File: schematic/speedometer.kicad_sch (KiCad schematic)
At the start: 11 parts

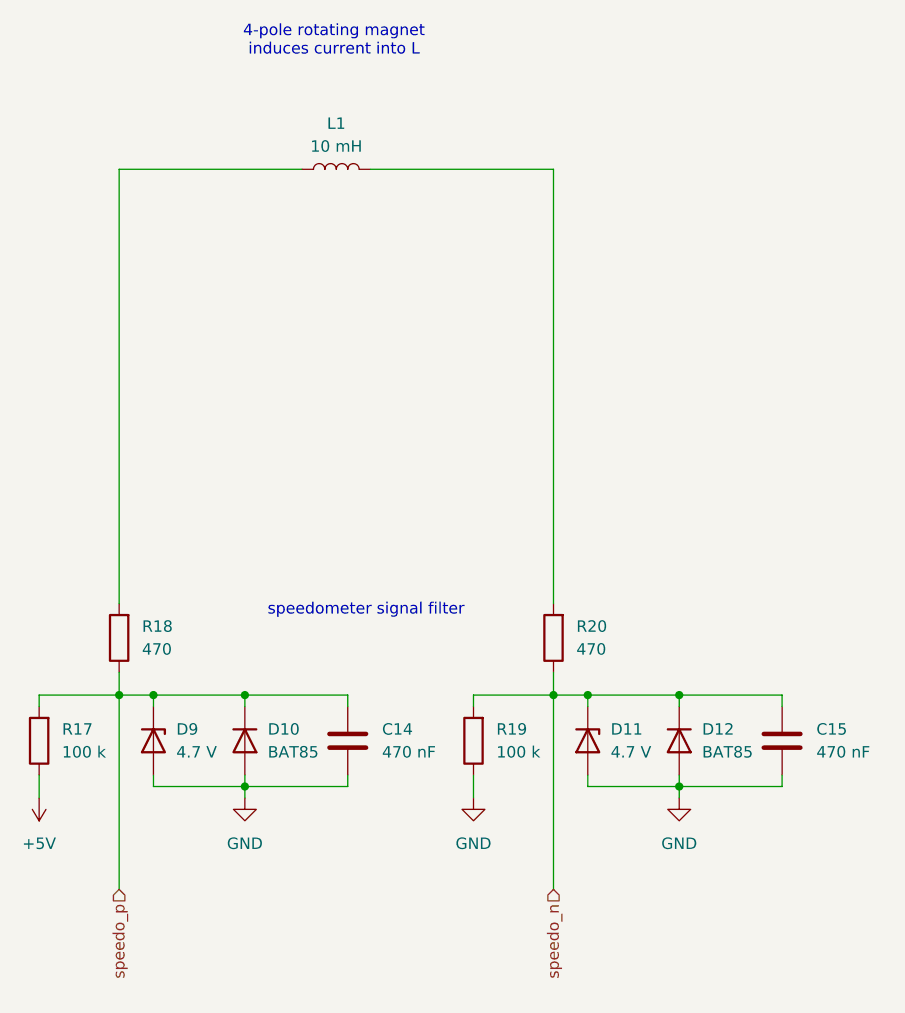
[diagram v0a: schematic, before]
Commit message: schematic: Add 2nd shutoff biasing
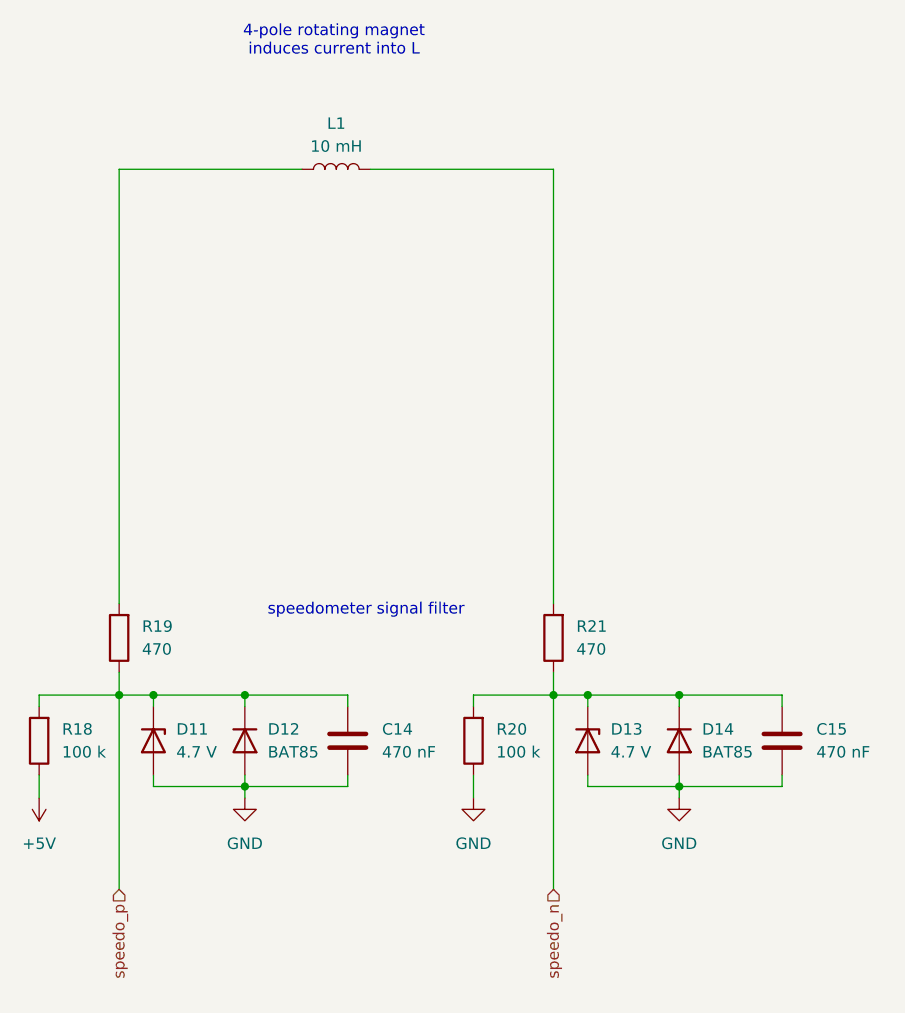
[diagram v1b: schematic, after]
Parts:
- renumbered D9 to D11, D10 to D12, D11 to D13, D12 to D14, R17 to R18, R18 to R19, R19 to R20, R20 to R21
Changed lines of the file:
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@@
 		(dnp no)
 		(fields_autoplaced yes)
-		(property "Reference" "#PWR022"
+		(property "Reference" "#PWR023"
 			(at 128.27 128.27 0)
 			(effects
@@
 			(project "phaseanglecontrol"
 				(path "/167e0419-9f88-4ea4-ae96-d03af9cd26b8/04a351f6-57f1-458a-8b72-1581301148b4"
-					(reference "#PWR022")
+					(reference "#PWR023")
 					(unit 1)
 				)
@@
 		(dnp no)
 		(fields_autoplaced yes)
-		(property "Reference" "D10"
+		(property "Reference" "D12"
 			(at 130.81 114.2999 90)
 			(effects
@@
 			(project "phaseanglecontrol"
 				(path "/167e0419-9f88-4ea4-ae96-d03af9cd26b8/04a351f6-57f1-458a-8b72-1581301148b4"
-					(reference "D10")
+					(reference "D12")
 					(unit 1)
 				)
@@
 		(dnp no)
 		(fields_autoplaced yes)
-		(property "Reference" "D9"
+		(property "Reference" "D11"
 			(at 120.65 114.2999 90)
 			(effects
@@
 			(project "phaseanglecontrol"
 				(path "/167e0419-9f88-4ea4-ae96-d03af9cd26b8/04a351f6-57f1-458a-8b72-1581301148b4"
-					(reference "D9")
+					(reference "D11")
 					(unit 1)
 				)
@@
 		(dnp no)
 		(fields_autoplaced yes)
-		(property "Reference" "#PWR023"
+		(property "Reference" "#PWR024"
 			(at 153.67 128.27 0)
 			(effects
@@
 			(project "phaseanglecontrol"
 				(path "/167e0419-9f88-4ea4-ae96-d03af9cd26b8/04a351f6-57f1-458a-8b72-1581301148b4"
-					(reference "#PWR023")
+					(reference "#PWR024")
 					(unit 1)
 				)
@@
 		(dnp no)
 		(fields_autoplaced yes)
-		(property "Reference" "R17"
+		(property "Reference" "R18"
 			(at 107.95 114.2999 0)
 			(effects
@@
 			(project "phaseanglecontrol"
 				(path "/167e0419-9f88-4ea4-ae96-d03af9cd26b8/04a351f6-57f1-458a-8b72-1581301148b4"
-					(reference "R17")
+					(reference "R18")
 					(unit 1)
 				)
@@
 		(dnp no)
 		(fields_autoplaced yes)
-		(property "Reference" "D11"
+		(property "Reference" "D13"
 			(at 168.91 114.2999 90)
 			(effects
@@
 			(project "phaseanglecontrol"
 				(path "/167e0419-9f88-4ea4-ae96-d03af9cd26b8/04a351f6-57f1-458a-8b72-1581301148b4"
-					(reference "D11")
+					(reference "D13")
 					(unit 1)
 				)
@@
 		(dnp no)
 		(fields_autoplaced yes)
-		(property "Reference" "R18"
+		(property "Reference" "R19"
 			(at 116.84 102.8699 0)
 			(effects
@@
 			(project "phaseanglecontrol"
 				(path "/167e0419-9f88-4ea4-ae96-d03af9cd26b8/04a351f6-57f1-458a-8b72-1581301148b4"
-					(reference "R18")
+					(reference "R19")
 					(unit 1)
 				)
@@
 		(dnp no)
 		(fields_autoplaced yes)
-		(property "Reference" "R20"
+		(property "Reference" "R21"
 			(at 165.1 102.8699 0)
 			(effects
@@
 			(project "phaseanglecontrol"
 				(path "/167e0419-9f88-4ea4-ae96-d03af9cd26b8/04a351f6-57f1-458a-8b72-1581301148b4"
-					(reference "R20")
+					(reference "R21")
 					(unit 1)
 				)
@@
 		(dnp no)
 		(fields_autoplaced yes)
-		(property "Reference" "#PWR021"
+		(property "Reference" "#PWR022"
 			(at 105.41 118.11 0)
 			(effects
@@
 			(project "phaseanglecontrol"
 				(path "/167e0419-9f88-4ea4-ae96-d03af9cd26b8/04a351f6-57f1-458a-8b72-1581301148b4"
-					(reference "#PWR021")
+					(reference "#PWR022")
 					(unit 1)
 				)
@@
 		(dnp no)
 		(fields_autoplaced yes)
-		(property "Reference" "D12"
+		(property "Reference" "D14"
 			(at 179.07 114.2999 90)
 			(effects
@@
 			(project "phaseanglecontrol"
 				(path "/167e0419-9f88-4ea4-ae96-d03af9cd26b8/04a351f6-57f1-458a-8b72-1581301148b4"
-					(reference "D12")
+					(reference "D14")
 					(unit 1)
 				)
@@
 		(dnp no)
 		(fields_autoplaced yes)
-		(property "Reference" "R19"
+		(property "Reference" "R20"
 			(at 156.21 114.2999 0)
 			(effects
@@
 			(project "phaseanglecontrol"
 				(path "/167e0419-9f88-4ea4-ae96-d03af9cd26b8/04a351f6-57f1-458a-8b72-1581301148b4"
-					(reference "R19")
+					(reference "R20")
 					(unit 1)
 				)
@@
 		(dnp no)
 		(fields_autoplaced yes)
-		(property "Reference" "#PWR024"
+		(property "Reference" "#PWR025"
 			(at 176.53 128.27 0)
 			(effects
@@
 			(project "phaseanglecontrol"
 				(path "/167e0419-9f88-4ea4-ae96-d03af9cd26b8/04a351f6-57f1-458a-8b72-1581301148b4"
-					(reference "#PWR024")
-					(unit 1)
-				)
+					(reference "#PWR025")
+					(unit 1)
+				)

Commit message: Add TVS to tirac gate
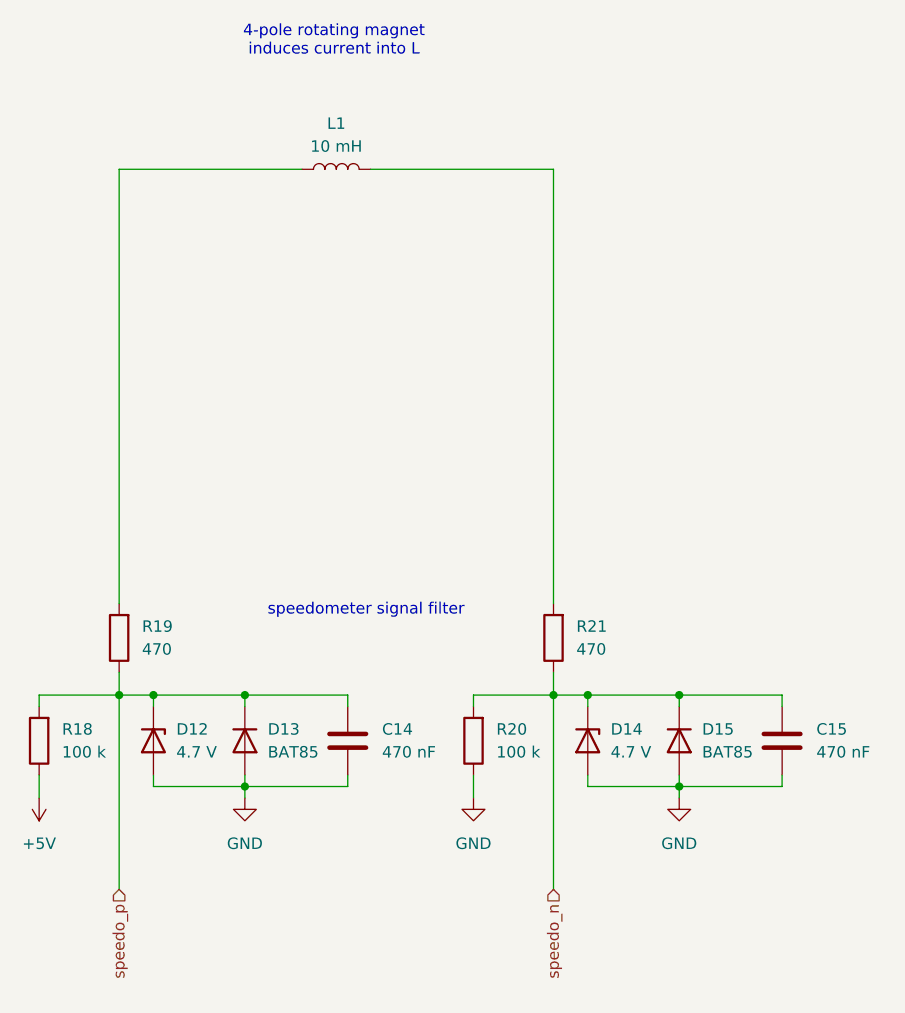
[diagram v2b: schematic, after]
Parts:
- renumbered D11 to D12, D12 to D13, D13 to D14, D14 to D15
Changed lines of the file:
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@@
 		(dnp no)
 		(fields_autoplaced yes)
-		(property "Reference" "#PWR023"
+		(property "Reference" "#PWR024"
 			(at 128.27 128.27 0)
 			(effects
@@
 			(project "phaseanglecontrol"
 				(path "/167e0419-9f88-4ea4-ae96-d03af9cd26b8/04a351f6-57f1-458a-8b72-1581301148b4"
-					(reference "#PWR023")
+					(reference "#PWR024")
 					(unit 1)
 				)
@@
 		(dnp no)
 		(fields_autoplaced yes)
-		(property "Reference" "D12"
+		(property "Reference" "D13"
 			(at 130.81 114.2999 90)
 			(effects
@@
 			(project "phaseanglecontrol"
 				(path "/167e0419-9f88-4ea4-ae96-d03af9cd26b8/04a351f6-57f1-458a-8b72-1581301148b4"
-					(reference "D12")
+					(reference "D13")
 					(unit 1)
 				)
@@
 		(dnp no)
 		(fields_autoplaced yes)
-		(property "Reference" "D11"
+		(property "Reference" "D12"
 			(at 120.65 114.2999 90)
 			(effects
@@
 			(project "phaseanglecontrol"
 				(path "/167e0419-9f88-4ea4-ae96-d03af9cd26b8/04a351f6-57f1-458a-8b72-1581301148b4"
-					(reference "D11")
+					(reference "D12")
 					(unit 1)
 				)
@@
 		(dnp no)
 		(fields_autoplaced yes)
-		(property "Reference" "#PWR024"
+		(property "Reference" "#PWR025"
 			(at 153.67 128.27 0)
 			(effects
@@
 			(project "phaseanglecontrol"
 				(path "/167e0419-9f88-4ea4-ae96-d03af9cd26b8/04a351f6-57f1-458a-8b72-1581301148b4"
-					(reference "#PWR024")
+					(reference "#PWR025")
 					(unit 1)
 				)
@@
 		(dnp no)
 		(fields_autoplaced yes)
-		(property "Reference" "D13"
+		(property "Reference" "D14"
 			(at 168.91 114.2999 90)
 			(effects
@@
 			(project "phaseanglecontrol"
 				(path "/167e0419-9f88-4ea4-ae96-d03af9cd26b8/04a351f6-57f1-458a-8b72-1581301148b4"
-					(reference "D13")
+					(reference "D14")
 					(unit 1)
 				)
@@
 		(dnp no)
 		(fields_autoplaced yes)
-		(property "Reference" "#PWR022"
+		(property "Reference" "#PWR023"
 			(at 105.41 118.11 0)
 			(effects
@@
 			(project "phaseanglecontrol"
 				(path "/167e0419-9f88-4ea4-ae96-d03af9cd26b8/04a351f6-57f1-458a-8b72-1581301148b4"
-					(reference "#PWR022")
+					(reference "#PWR023")
 					(unit 1)
 				)
@@
 		(dnp no)
 		(fields_autoplaced yes)
-		(property "Reference" "D14"
+		(property "Reference" "D15"
 			(at 179.07 114.2999 90)
 			(effects
@@
 			(project "phaseanglecontrol"
 				(path "/167e0419-9f88-4ea4-ae96-d03af9cd26b8/04a351f6-57f1-458a-8b72-1581301148b4"
-					(reference "D14")
+					(reference "D15")
 					(unit 1)
 				)
@@
 		(dnp no)
 		(fields_autoplaced yes)
-		(property "Reference" "#PWR025"
+		(property "Reference" "#PWR026"
 			(at 176.53 128.27 0)
 			(effects
@@
 			(project "phaseanglecontrol"
 				(path "/167e0419-9f88-4ea4-ae96-d03af9cd26b8/04a351f6-57f1-458a-8b72-1581301148b4"
-					(reference "#PWR025")
-					(unit 1)
-				)
+					(reference "#PWR026")
+					(unit 1)
+				)
